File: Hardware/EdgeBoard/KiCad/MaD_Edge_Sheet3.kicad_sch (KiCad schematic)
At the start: 46 parts, among them IC14 ISO6741DWR, IC15 ISO6721BDR, IC16 ISO6740FDWR, J20 Encoder, J21 ServoCtrl, J23 ServoSerial, Q1 NPN, U24 AM26LS31CD, U25 AM26LV32xD, U27 SN74LVC1G14DBV, U28 SN74LVC1G14DBV, U29 SN74LVC1G14DBV, U30 SN74LVC1G14DBV, U31 SN74LVC1G14DBV, U32 SN74LVC1G14DBV, U33 SN74LVC1G14DBV, U34 SN74LVC1G14DBV

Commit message: fix(hardware): U25's part number is the AM26LV32IDR it was bought as
U25 on the Edge carrier is the AM26LV32 RS-422 line receiver: its symbol
is Interface:AM26LV32xD, its LCSC part is C524786 (AM26LV32IDR), and its
manufacturer_part_number_1 says AM26LV32IDR, in the schematic and on the
PCB. Its Manufacturer_Part_Number said AM26LS32CD, a different receiver,
and its Value the symbol's generic AM26LV32xD. Both now say AM26LV32IDR.

A netlist exported from the schematic now names the part a simulation
places by its number (embsim's am26lv32 kind, embsim MIGRATING-MAD.md E1).
Only the schematic's two properties change; the PCB footprint's own
Value and Manufacturer_Part_Number follow on the next "Update PCB from
Schematic".

Co-Authored-By: Claude Opus 5.5 <noreply@anthropic.com>
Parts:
- U25: value AM26LV32xD -> AM26LV32IDR; Manufacturer_Part_Number AM26LS32CD -> AM26LV32IDR
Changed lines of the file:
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@@
 			)
 		)
-		(property "Value" "AM26LV32xD"
+		(property "Value" "AM26LV32IDR"
 			(at 105.41 130.81 0)
 			(effects
@@
 			)
 		)
-		(property "Manufacturer_Part_Number" "AM26LS32CD"
+		(property "Manufacturer_Part_Number" "AM26LV32IDR"
 			(at 110.49 134.62 0)
 			(effects

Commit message: fix(hardware): ground IC14's drive side (GND2) to EN_GND on the Edge board
IC14 (ISO6741DWR, the servo STEP/DIR/ENA/SRDY isolator) had its GND2 pins
9 and 15 on an isolated net, Net-(IC14-GND2_1), with only C26: no EN_GND
in the schematic and no connection to the EN_GND pour in the layout. As
drawn, the drive-side half of the isolator had no ground return.

Schematic: an EN_GND label on GND2's wire puts pins 9 and 15 and C26.2 on
EN_GND with J21.8 and the rest of the drive side.

Layout: the 3 pads, 10 traces and 2 vias of the old net move to EN_GND.
Both vias already sit inside the In1.Cu EN_GND pour, which is refilled so
it now joins them. The file stays in KiCad 9 format for KiBot; the new
fill was computed by KiCad 10 and matches a fresh refill exactly.

DRC: 0 unconnected; net_conflict 4 -> 1; schematic parity 105 -> 102;
other violations unchanged. ERC errors unchanged (9, all pre-existing).

Co-Authored-By: Claude Opus 5.5 <noreply@anthropic.com>
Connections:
- net EN_GND: now also C26.2, IC14.15 (GND2_2), IC14.9 (GND2_1)
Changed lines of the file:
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@@
+	)
+	(label "EN_GND"
+		(at 76.2 68.58 0)
+		(effects
+			(font
+				(size 1.27 1.27)
+			)
+			(justify left bottom)
+		)
 	)
 	(label "EN_GND"

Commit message: fix(hardware): servo enable off at power-up: IC14 ISO7741FDWR and a P6 pull-down
Finding SRV-F6. Nothing pulls P6 (servo enable request), and the fitted
non-F IC14 outputs high from an open or unpowered input, so the drive
enable is on through reset, boot and flashing.

- IC14 becomes ISO7741FDWR (LCSC C485810): same pinout (TI SLLSEP4K
  Table 4-1 p.5); with the F suffix an open input or an unpowered side 1
  gives a low output (Table 7-2 p.29). Value, MPN, LCSC and notes updated.
- R39, 10 k (0603WAF1002T5E, C25804) from P6 to GND. On the PCB it sits
  by IC14 and joins the P6 trace at U29 through two 0.6 mm vias and B.Cu.
- STEP/DIR (P8/P7) now also rest low when undriven.

Co-Authored-By: Claude Opus 5.5 <noreply@anthropic.com>
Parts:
- added R39: 10K, Resistor_SMD:R_0603_1608Metric, symbol Device:R_Small
- IC14: value ISO6741DWR -> ISO7741FDWR; DIGIKEY 296-ISO6741DWRCT-ND -> (none); LCSC C571196 -> C485810; Manufacturer_Part_Number ISO6741DWR -> ISO7741FDWR; NOTES Pin Compatible with ISO77xx -> F suffix required: outputs default LOW with an open input o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; Qty Bought 3 - lcsc -> (none); manufacturer_part_number_1 ISO6741DWR or ISO7741DWR -> ISO7741FDWR
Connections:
- net GND: now also R39.2
- net P6: now also R39.1
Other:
- note added: "R39 holds P6 low: servo enable off through reset, boot and flashing. IC14 is an F part: outputs default low if side 1 is unpowered."

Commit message: fix(hardware): Q1 drawn and laid out as the fitted SOT-23 MMBT3904
Finding SRV-F8-Q1. Q1 used the TO-92 2N3904 symbol (1 E, 2 B, 3 C) but
the part fitted is a SOT-23 MMBT3904 (1 B, 2 E, 3 C; JSCJ datasheet,
LCSC C20526, p.1), so JP1's open-collector position could never enable
the drive.

- Symbol Transistor_BJT:MMBT3904, footprint Package_TO_SOT_SMD:SOT-23.
- PCB: Q1 rotated -90 so base faces R24; base to R24, emitter to a new
  EN_GND via, collector to JP1 pin 3. The old emitter trace and via go.

Co-Authored-By: Claude Opus 5.5 <noreply@anthropic.com>
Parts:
- Q1: value NPN -> MMBT3904; footprint Package_TO_SOT_SMD:TSOT-23 -> Package_TO_SOT_SMD:SOT-23; symbol Transistor_BJT:2N3904 -> Transistor_BJT:MMBT3904; NOTES (none) -> SOT-23 pinout 1 B, 2 E, 3 C (JSCJ MMBT3904 datasheet p.1)
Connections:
- net EN_GND: now also Q1.2 (E); no longer Q1.1 (E)
- net at R24.2: now also Q1.1 (B); no longer Q1.2 (B)
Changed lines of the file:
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@@
 	)
 	(symbol
-		(lib_id "Transistor_BJT:2N3904")
+		(lib_id "Transistor_BJT:MMBT3904")
 		(at 77.47 91.44 0)
 		(unit 1)
@@
 			)
 		)
-		(property "Value" "NPN"
+		(property "Value" "MMBT3904"
 			(at 82.55 92.7099 0)
 			(effects
@@
 			)
 		)
-		(property "Footprint" "Package_TO_SOT_SMD:TSOT-23"
+		(property "Footprint" "Package_TO_SOT_SMD:SOT-23"
 			(at 82.55 93.345 0)
 			(effects
@@
 			)
 		)
-		(property "Datasheet" "https://www.onsemi.com/pub/Collateral/2N3903-D.PDF"
+		(property "Datasheet" "https://www.lcsc.com/datasheet/C20526.pdf"
 			(at 77.47 91.44 0)
 			(effects
@@
 			)
 		)
-		(property "NOTES" ""
+		(property "NOTES" "SOT-23 pinout 1 B, 2 E, 3 C (JSCJ MMBT3904 datasheet p.1)"
 			(at 77.47 91.44 0)
 			(effects

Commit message: fix(hardware): U25 AM26C32IDR (5 V receiver) with its own 0.1 uF
Finding ENC-F3. U25 (AM26LV32IDR, 3.0-3.6 V, TI SLLS202H 6.3) runs from
the 5 V SC_5V rail.

- U25 becomes AM26C32IDR (LCSC C36693): pin-identical (TI SLLS104M
  Table 4-1 p.3), VCC 4.5-5.5 V (5.3 p.4), VOH >= 3.8 V at -6 mA (5.6
  p.5), above IC16's 0.7 x VCC1 input threshold. KiCad has no AM26C32
  symbol; the AM26LV32xD symbol stays.
- C30, 0.1 uF 0402 (CL05B104KO5NNNC, C1525) from U25.16 to EN_GND,
  beside the pin. 0402 is the size that fits between JP2 and U25.

Co-Authored-By: Claude Opus 5.5 <noreply@anthropic.com>
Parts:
- added C30: 0.1uF, Capacitor_SMD:C_0402_1005Metric, symbol Device:C_Small
- U25: value AM26LV32IDR -> AM26C32IDR; LCSC C524786 -> C36693; Manufacturer_Part_Number AM26LV32IDR -> AM26C32IDR; NOTES (none) -> Must be a 5 V receiver (AM26C32, VCC 4.5-5.5 V, VOH >= 3.8 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; Qty Bought 3 lcsc -> (none); manufacturer_part_number_1 AM26LV32IDR -> AM26C32IDR
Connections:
- net EN_GND: now also C30.2
- net SC_5V: now also C30.1
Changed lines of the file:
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@@
 			)
 		)
-		(property "Value" "AM26LV32IDR"
+		(property "Value" "AM26C32IDR"
 			(at 105.41 130.81 0)
 			(effects
@@
 			)
 		)
-		(property "Datasheet" "http://www.ti.com/lit/ds/symlink/am26lv32.pdf"
+		(property "Datasheet" "https://www.ti.com/lit/ds/symlink/am26c32.pdf"
 			(at 110.49 144.78 0)
 			(effects
@@
 			)
 		)
-		(property "Description" "IC RECEIVER 0/4 16SOIC"
+		(property "Description" "Quad differential line receiver, 5 V, SOIC-16"
 			(at 110.49 134.62 0)
 			(effects
@@
 			)
 		)
-		(property "Manufacturer_Part_Number" "AM26LV32IDR"
+		(property "Manufacturer_Part_Number" "AM26C32IDR"
 			(at 110.49 134.62 0)
 			(effects
@@
 			)
 		)
-		(property "LCSC" "C524786"
+		(property "LCSC" "C36693"
 			(at 110.49 134.62 0)
 			(effects
@@
 			)
 		)
-		(property "NOTES" ""
+		(property "NOTES" "Must be a 5 V receiver (AM26C32, VCC 4.5-5.5 V, VOH >= 3.8 V). Not AM26LV32 (3.6 V max) or AM26LS32 (VOH 2.7 V). Symbol is AM26LV32xD: same pinout."
 			(at 110.49 134.62 0)
 			(effects
@@
 			)
 		)
-		(property "manufacturer_part_number_1" "AM26LV32IDR"
+		(property "manufacturer_part_number_1" "AM26C32IDR"
 			(at 110.49 134.62 0)
 			(effects
@@
 			)
 		)
-		(property "Qty Bought" "3 lcsc"
+		(property "Qty Bought" ""
 			(at 110.49 134.62 0)
 			(effects
@@
 		)
 	)
+	(symbol
+		(lib_id "Device:C_Small")
+		(at 231.14 110.49 0)
+		(unit 1)
+		(exclude_from_sim no)
+		(in_bom yes)
+		(on_board yes)
+		(dnp no)
+		(property "Reference" "C30"
+			(at 233.68 109.2262 0)
+			(effects
+				(font
+					(size 1.27 1.27)
+				)
+				(justify left)
+			)
+		)
+		(property "Value" "0.1uF"
+			(at 233.68 111.76 0)
+			(effects
+				(font
+					(size 1.27 1.27)
+				)
+				(justify left)
+			)
+		)
+		(property "Footprint" "Capacitor_SMD:C_0402_1005Metric"
+			(at 231.14 110.49 0)
+			(effects
+				(font
+					(size 1.27 1.27)
+				)
+				(hide yes)
+			)
+		)
+		(property "Datasheet" "~"
+			(at 231.14 110.49 0)
+			(effects
+				(font
+					(size 1.27 1.27)
+				)
+				(hide yes)
+			)
+		)
+		(property "Description" "0.1uF 16V X7R 0402"
+			(at 231.14 110.49 0)
+			(effects
+				(font
+					(size 1.27 1.27)
+				)
+				(hide yes)
+			)
+		)
+		(property "MANUFACTURER" "Samsung Electro-Mechanics"
+			(at 231.14 110.49 0)
+			(effects
+				(font
+					(size 1.27 1.27)
+				)
+				(hide yes)
+			)
+		)
+		(property "Manufacturer_Part_Number" "CL05B104KO5NNNC"
+			(at 231.14 110.49 0)
+			(effects
+				(font
+					(size 1.27 1.27)
+				)
+				(hide yes)
+			)
+		)
+		(property "DIGIKEY" ""
+			(at 231.14 110.49 0)
+			(effects
+				(font
+					(size 1.27 1.27)
+				)
+				(hide yes)
+			)
+		)
+		(property "LCSC" "C1525"
+			(at 231.14 110.49 0)
+			(effects
+				(font
+					(size 1.27 1.27)
+				)
+				(hide yes)
+			)
+		)
+		(property "NOTES" "U25 decoupling: place at U25 pin 16 (0402 to fit beside JP2)"
+			(at 231.14 110.49 0)
+			(effects
+				(font
+					(size 1.27 1.27)
+				)
+				(hide yes)
+			)
+		)
+		(property "manufacturer_1" "Samsung Electro-Mechanics"
+			(at 231.14 110.49 0)
+			(effects
+				(font
+					(size 1.27 1.27)
+				)
+				(hide yes)
+			)
+		)
+		(property "manufacturer_part_number_1" "CL05B104KO5NNNC"
+			(at 231.14 110.49 0)
+			(effects
+				(font
+					(size 1.27 1.27)
+				)
+				(hide yes)
+			)
+		)
+		(property "Qty Bought" ""
+			(at 231.14 110.49 0)
+			(effects
+				(font
+					(size 1.27 1.27)
+				)
+				(hide yes)
+			)
+		)
+		(property "Receptical" ""
+			(at 231.14 110.49 0)
+			(effects
+				(font
+					(size 1.27 1.27)
+				)
+				(hide yes)
+			)
+		)
+		(pin "1"
+		)
+		(pin "2"
+		)
+		(instances
+			(project "MaD_Edge"
+				(path "/7e1266c3-436e-48c1-8e6f-07c0e2581bd5/3848150c-e17f-4b7c-8b45-f477f8e036d7"
+					(reference "C30")
+					(unit 1)
+				)
+			)
+		)
+	)
+	(wire
+		(pts
+			(xy 231.14 107.95) (xy 231.14 105.41)
+		)
+		(stroke
+			(width 0)
+			(type default)
+		)
+	)
+	(label "SC_5V"
+		(at 231.14 105.41 90)
+		(effects
+			(font
+				(size 1.27 1.27)
+			)
+			(justify left bottom)
+		)
+	)
+	(wire
+		(pts
+			(xy 231.14 113.03) (xy 231.14 115.57)
+		)
+		(stroke
+			(width 0)
+			(type default)
+		)
+	)
+	(label "EN_GND"
+		(at 231.14 115.57 270)
+		(effects
+			(font
+				(size 1.27 1.27)
+			)
+			(justify right bottom)
+		)
+	)

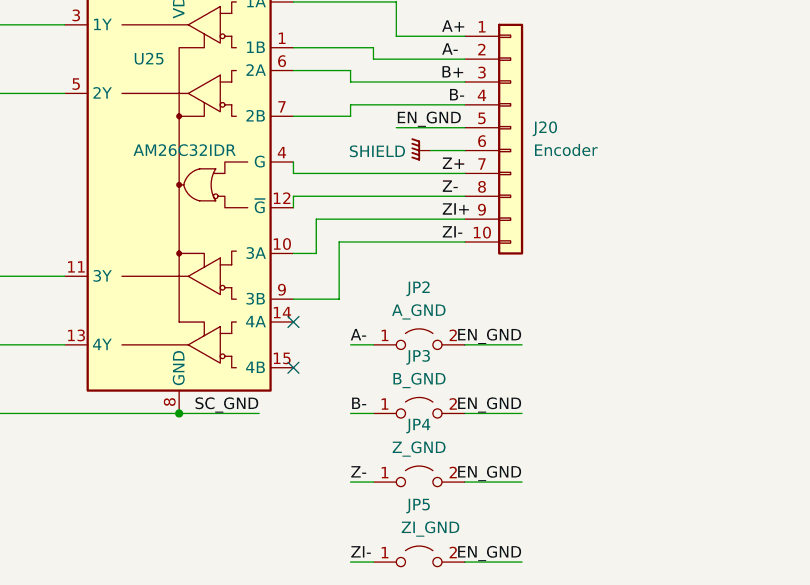
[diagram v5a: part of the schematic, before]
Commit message: fix(hardware): U25 always enabled; Z+/Z- on receiver 4; JP4 removed
Finding ENC-F5. U25's enables (G pin 4, ~G pin 12) were wired to J20's
Z+/Z-, so they needed a shunt on JP4 that the BOM did not have, and
receiver 4 was unused.

- G to SC_5V, ~G to EN_GND (SLLS104M Table 7-1 p.9): always enabled.
  The two under-body vias are re-netted to the In2/In1 planes.
- Z+/Z- (J20.7/.8) to 4A/4B (pins 14/15); 4Y reaches P12 through IC16
  channel D. New B.Cu routes and two vias under U25, clear of the
  IC16-INA/INB traces that cross the body.
- JP4 deleted (schematic and PCB).

Co-Authored-By: Claude Opus 5.5 <noreply@anthropic.com>
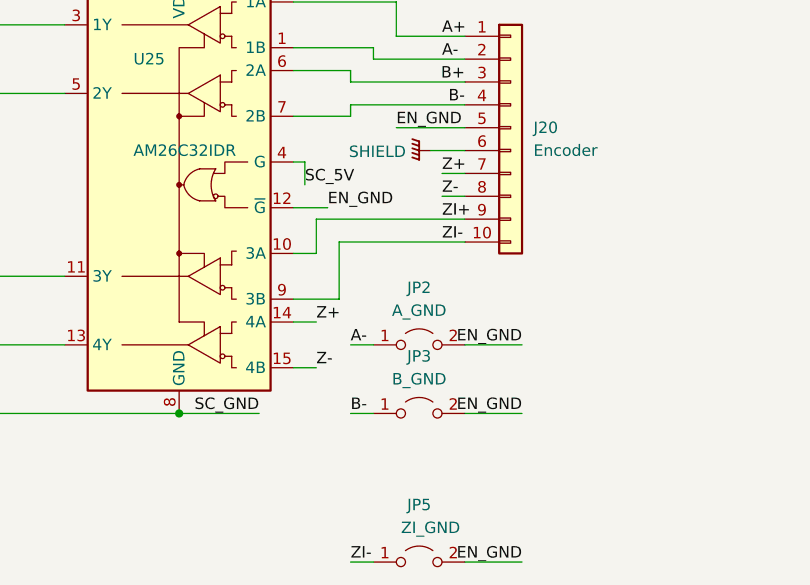
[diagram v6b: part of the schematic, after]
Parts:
- removed JP4: Z_GND, Connector_PinHeader_2.54mm:PinHeader_1x02_P2.54mm_Vertical, symbol Jumper:Jumper_2_Open
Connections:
- net EN_GND: now also U25.12 (~{G})
- net SC_5V: now also U25.4 (G)
- net Z+: now also U25.14 (4A); no longer U25.4 (G)
- net Z-: now also U25.15 (4B); no longer U25.12 (~{G})
- no-connect marks 11 -> 9
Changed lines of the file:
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@@
 	)
 	(no_connect
-		(at 123.19 154.94)
-	)
-	(no_connect
-		(at 123.19 149.86)
-	)
-	(no_connect
 		(at 40.64 139.7)
 	)
@@
 	(wire
 		(pts
-			(xy 129.54 167.64) (xy 132.08 167.64)
-		)
-		(stroke
-			(width 0)
-			(type default)
-		)
-	)
-	(wire
-		(pts
 			(xy 148.59 152.4) (xy 142.24 152.4)
 		)
@@
 	(wire
 		(pts
-			(xy 123.19 135.89) (xy 123.19 137.16)
-		)
-		(stroke
-			(width 0)
-			(type default)
-		)
-	)
-	(wire
-		(pts
 			(xy 142.24 138.43) (xy 125.73 138.43)
 		)
@@
 	(wire
 		(pts
-			(xy 148.59 167.64) (xy 142.24 167.64)
-		)
-		(stroke
-			(width 0)
-			(type default)
-		)
-	)
-	(wire
-		(pts
 			(xy 73.66 132.08) (xy 87.63 132.08)
 		)
@@
 	(wire
 		(pts
-			(xy 142.24 133.35) (xy 123.19 133.35)
+			(xy 142.24 133.35) (xy 139.7 133.35)
 		)
 		(stroke
@@
 	(wire
 		(pts
-			(xy 142.24 135.89) (xy 123.19 135.89)
+			(xy 142.24 135.89) (xy 139.7 135.89)
 		)
 		(stroke
@@
 	(wire
 		(pts
-			(xy 123.19 133.35) (xy 123.19 132.08)
-		)
-		(stroke
-			(width 0)
-			(type default)
-		)
-	)
-	(wire
-		(pts
 			(xy 121.92 60.96) (xy 142.24 60.96)
 		)
@@
 		)
 	)
-	(label "Z-"
-		(at 129.54 167.64 0)
-		(effects
-			(font
-				(size 1.27 1.27)
-			)
-			(justify left bottom)
-		)
-	)
 	(label "ZI+"
 		(at 139.7 138.43 0)
@@
 		)
 	)
-	(label "EN_GND"
-		(at 148.59 167.64 180)
-		(effects
-			(font
-				(size 1.27 1.27)
-			)
-			(justify right bottom)
-		)
-	)
 	(label "ISS_5V"
 		(at 139.065 25.4 0)
@@
 	)
 	(symbol
-		(lib_id "Jumper:Jumper_2_Open")
-		(at 137.16 167.64 0)
-		(unit 1)
-		(exclude_from_sim no)
-		(in_bom yes)
-		(on_board yes)
-		(dnp no)
-		(fields_autoplaced yes)
-		(property "Reference" "JP4"
-			(at 137.16 161.29 0)
-			(effects
-				(font
-					(size 1.27 1.27)
-				)
-			)
-		)
-		(property "Value" "Z_GND"
-			(at 137.16 163.83 0)
-			(effects
-				(font
-					(size 1.27 1.27)
-				)
-			)
-		)
-		(property "Footprint" "Connector_PinHeader_2.54mm:PinHeader_1x02_P2.54mm_Vertical"
-			(at 137.16 167.64 0)
-			(effects
-				(font
-					(size 1.27 1.27)
-				)
-				(hide yes)
-			)
-		)
-		(property "Datasheet" "~"
-			(at 137.16 167.64 0)
-			(effects
-				(font
-					(size 1.27 1.27)
-				)
-				(hide yes)
-			)
-		)
-		(property "Description" "~"
-			(at 137.16 167.64 0)
-			(effects
-				(font
-					(size 1.27 1.27)
-				)
-				(hide yes)
-			)
-		)
-		(property "MANUFACTURER" "~"
-			(at 137.16 167.64 0)
-			(effects
-				(font
-					(size 1.27 1.27)
-				)
-				(hide yes)
-			)
-		)
-		(property "Manufacturer_Part_Number" "~"
-			(at 137.16 167.64 0)
-			(effects
-				(font
-					(size 1.27 1.27)
-				)
-				(hide yes)
-			)
-		)
-		(property "DIGIKEY" "~"
-			(at 137.16 167.64 0)
-			(effects
-				(font
-					(size 1.27 1.27)
-				)
-				(hide yes)
-			)
-		)
-		(property "LCSC" "C492401"
-			(at 137.16 167.64 0)
-			(effects
-				(font
-					(size 1.27 1.27)
-				)
-				(hide yes)
-			)
-		)
-		(property "NOTES" ""
-			(at 137.16 167.64 0)
-			(effects
-				(font
-					(size 1.27 1.27)
-				)
-				(hide yes)
-			)
-		)
-		(property "manufacturer_1" "XFCN"
-			(at 137.16 167.64 0)
-			(effects
-				(font
-					(size 1.27 1.27)
-				)
-				(hide yes)
-			)
-		)
-		(property "manufacturer_part_number_1" "PZ254V-11-02P"
-			(at 137.16 167.64 0)
-			(effects
-				(font
-					(size 1.27 1.27)
-				)
-				(hide yes)
-			)
-		)
-		(property "Qty Bought" "header"
-			(at 137.16 167.64 0)
-			(effects
-				(font
-					(size 1.27 1.27)
-				)
-				(hide yes)
-			)
-		)
-		(property "Receptical" ""
-			(at 137.16 167.64 0)
-			(effects
-				(font
-					(size 1.27 1.27)
-				)
-				(hide yes)
-			)
-		)
-		(pin "1"
-		)
-		(pin "2"
-		)
-		(instances
-			(project "MaD_Edge"
-				(path "/7e1266c3-436e-48c1-8e6f-07c0e2581bd5/3848150c-e17f-4b7c-8b45-f477f8e036d7"
-					(reference "JP4")
-					(unit 1)
-				)
-			)
-		)
-	)
-	(symbol
 		(lib_id "power:GND")
 		(at 213.36 85.09 0)
@@
 		)
 	)
+	(wire
+		(pts
+			(xy 123.19 132.08) (xy 124.46 132.08)
+		)
+		(stroke
+			(width 0)
+			(type default)
+		)
+	)
+	(wire
+		(pts
+			(xy 124.46 132.08) (xy 124.46 134.62)
+		)
+		(stroke
+			(width 0)
+			(type default)
+		)
+	)
+	(label "SC_5V"
+		(at 124.46 134.62 0)
+		(effects
+			(font
+				(size 1.27 1.27)
+			)
+			(justify left bottom)
+		)
+	)
+	(wire
+		(pts
+			(xy 123.19 137.16) (xy 127 137.16)
+		)
+		(stroke
+			(width 0)
+			(type default)
+		)
+	)
+	(label "EN_GND"
+		(at 127 137.16 0)
+		(effects
+			(font
+				(size 1.27 1.27)
+			)
+			(justify left bottom)
+		)
+	)
+	(wire
+		(pts
+			(xy 123.19 149.86) (xy 125.73 149.86)
+		)
+		(stroke
+			(width 0)
+			(type default)
+		)
+	)
+	(label "Z+"
+		(at 125.73 149.86 0)
+		(effects
+			(font
+				(size 1.27 1.27)
+			)
+			(justify left bottom)
+		)
+	)
+	(wire
+		(pts
+			(xy 123.19 154.94) (xy 125.73 154.94)
+		)
+		(stroke
+			(width 0)
+			(type default)
+		)
+	)
+	(label "Z-"
+		(at 125.73 154.94 0)
+		(effects
+			(font
+				(size 1.27 1.27)
+			)
+			(justify left bottom)
+		)
+	)
